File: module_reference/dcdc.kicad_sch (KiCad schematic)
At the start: 59 parts, among them J301 Conn_01x01, J302 Conn_01x01, J303 Conn_01x01, J304 Conn_01x01, J305 Conn_01x01, Q301 MMBT3904, T301 Feryster RTN-40x25x15(M-083), U301 L78L33_SOT89, U302 LT3439, U303 24AA02-OT, U304 TMP117, U305 LT3045xMSE

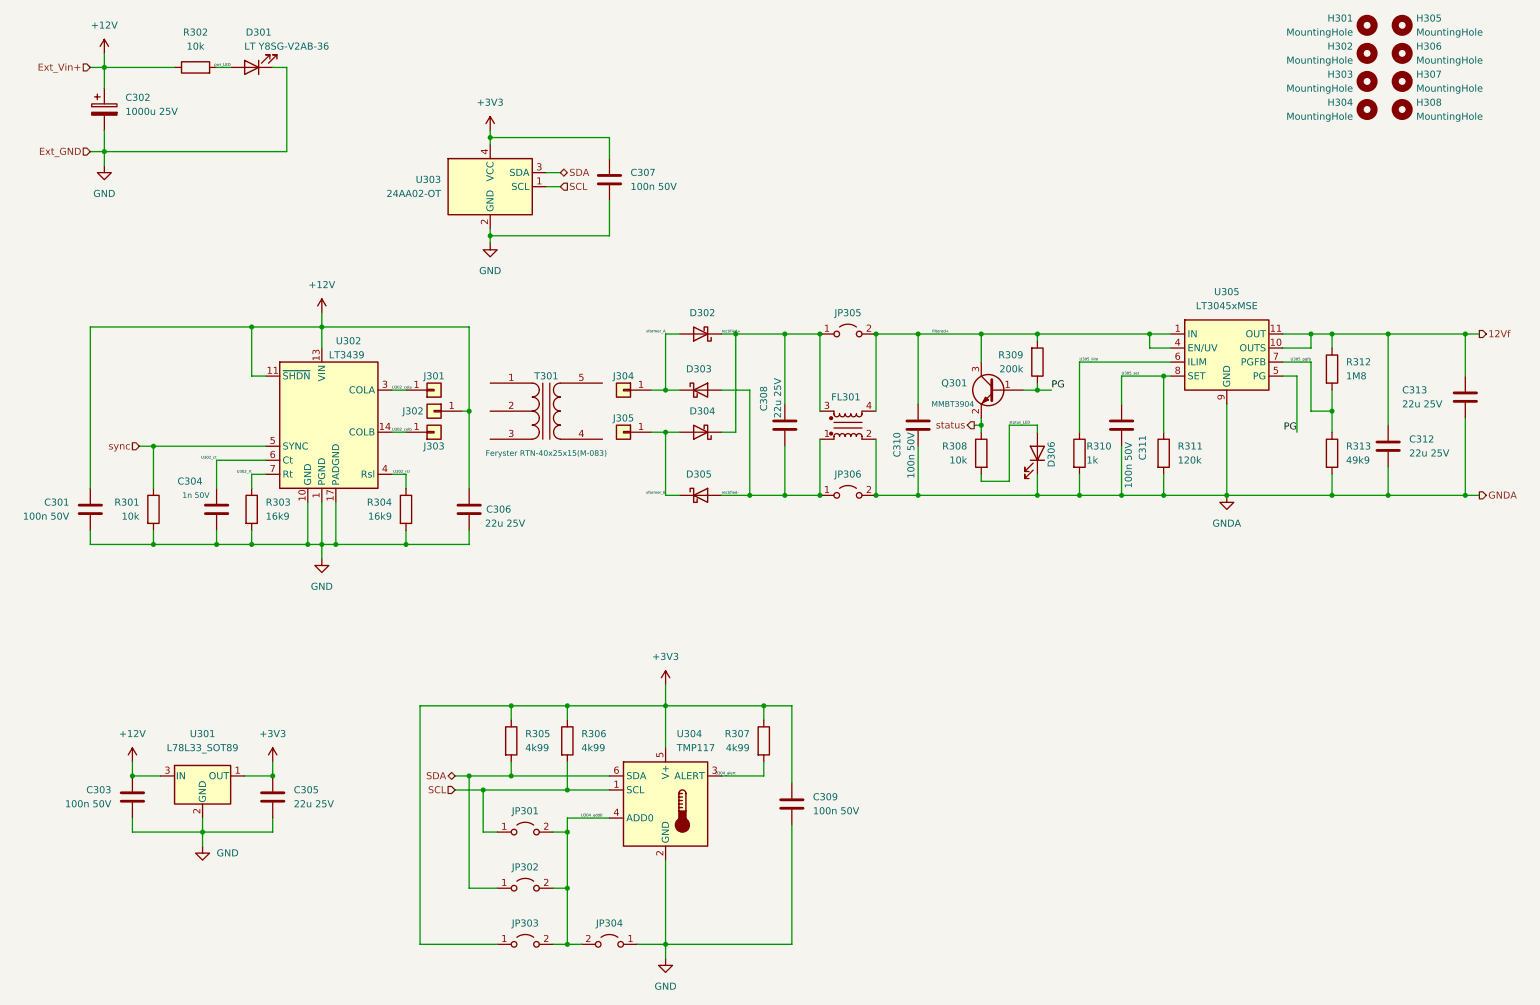
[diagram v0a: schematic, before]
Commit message: switched to addressable eeprom
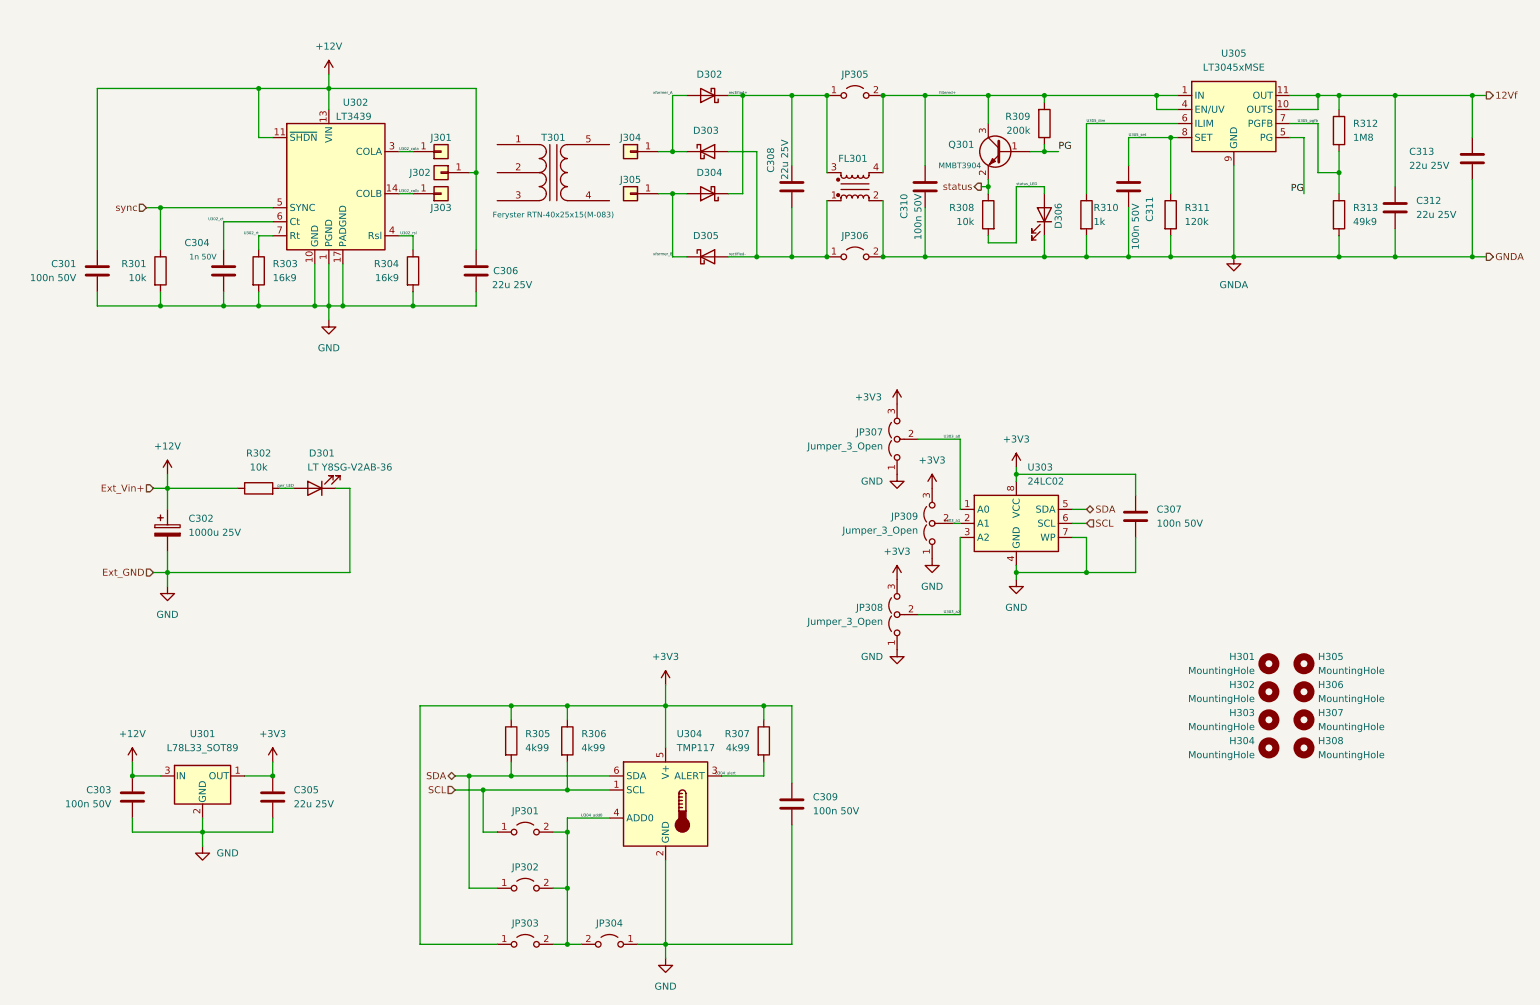
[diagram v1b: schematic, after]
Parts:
- removed U303: 24AA02-OT, Package_TO_SOT_SMD:SOT-23-5, symbol Memory_EEPROM:24AA02-OT
- added JP307, JP308, JP309: Jumper_3_Open, Jumper:SolderJumper-3_P1.3mm_Open_RoundedPad1.0x1.5mm_NumberLabels, symbol Jumper:Jumper_3_Open
- added U303: 24LC02, Package_SO:MSOP-8_3x3mm_P0.65mm, symbol Memory_EEPROM:24LC02
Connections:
- net +3V3: now also JP307.3 (B), JP308.3 (B), JP309.3 (B), U303.8 (VCC)
- net GND: now also JP307.1 (A), JP308.1 (A), JP309.1 (A), U303.4 (GND), U303.7 (WP)
- net SCL: now also U303.6 (SCL)
- net SDA: now also U303.5 (SDA)
- new net U303_a0: JP307.2 (C), U303.1 (A0)
- new net U303_a1: JP309.2 (C), U303.2 (A1)
- new net U303_a2: JP308.2 (C), U303.3 (A2)
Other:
- moved on the sheet: C301, C302, C304, C306, C307, C308, C310, C311, C312, C313, D301, D302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

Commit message: rev 0.4 layout step
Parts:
- removed FL301: B82793C0206N265, ADRmu_Library:Filter_EPCOS_B82793C0, symbol Device:Filter_EMI_CommonMode
- removed JP305, JP306: Jumper_2_Open, Jumper:SolderJumper-2_P1.3mm_Open_RoundedPad1.0x1.5mm, symbol Jumper:Jumper_2_Open
- renumbered C303 to C302, C302 to C303, C308 to C307, C309 to C308, C310 to C309, C311 to C310, C307 to C311, R303 to R302, R302 to R303, U304 to U303, U303 to U304
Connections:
- net rectified+ is gone; now on net filtered+: C307.1, D302.1 (K), D304.1 (K)
- net rectified- is gone; now on net GNDA: C307.2, D303.2 (A), D305.2 (A)
- no-connect marks 0 -> 5
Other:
- moved on the sheet: C309, C310, C312, C313, D306, Q301, R308, R309, R310, R311, R312, R313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

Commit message: asdf
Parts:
- JP307, JP308, JP309: now left out of the parts list
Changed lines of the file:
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@@
   (title_block
     (title "DC-DC converter & misc")
-    (date "2022-03-02")
+    (date "2022-03-04")
     (rev "0.4")
     (company "RPG")
@@
   )
   (symbol (lib_id "Jumper:Jumper_3_Open") (at 171.45 92.71 90) (unit 1)
-    (in_bom yes) (on_board yes) (fields_autoplaced)
+    (in_bom no) (on_board yes) (fields_autoplaced)
     (property "Reference" "JP307" (id 0) (at 168.91 91.4399 90)
       (effects (font (size 1.27 1.27)) (justify left))
@@
   )
   (symbol (lib_id "Jumper:Jumper_3_Open") (at 177.8 107.95 90) (unit 1)
-    (in_bom yes) (on_board yes) (fields_autoplaced)
+    (in_bom no) (on_board yes) (fields_autoplaced)
     (property "Reference" "JP309" (id 0) (at 175.26 106.6799 90)
       (effects (font (size 1.27 1.27)) (justify left))
@@
   )
   (symbol (lib_id "Jumper:Jumper_3_Open") (at 171.45 124.46 90) (unit 1)
-    (in_bom yes) (on_board yes) (fields_autoplaced)
+    (in_bom no) (on_board yes) (fields_autoplaced)
     (property "Reference" "JP308" (id 0) (at 168.91 123.1899 90)
       (effects (font (size 1.27 1.27)) (justify left))

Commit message: dimmed LED brightness and started to fix a few first generation battery bug fixes
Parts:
- R303, R308: value 10k -> 16k9
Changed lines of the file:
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@@
     (in_bom yes) (on_board yes) (fields_autoplaced)
     (property "Reference" "R303" (id 0) (at 55.88 95.25 90))
-    (property "Value" "10k" (id 1) (at 55.88 97.79 90))
+    (property "Value" "16k9" (id 1) (at 55.88 97.79 90))
     (property "Footprint" "Resistor_SMD:R_0805_2012Metric" (id 2) (at 55.88 103.378 90)
       (effects (font (size 1.27 1.27)) hide)
@@
       (effects (font (size 1.27 1.27)) (justify left))
     )
-    (property "Value" "10k" (id 1) (at 168.91 53.3399 0)
-      (effects (font (size 1.27 1.27)) (justify left))
-    )
+    (property "Value" "16k9" (id 1) (at 168.91 53.3399 0)
+      (effects (font (size 1.27 1.27)) (justify left))
+    )

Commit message: Battery module Rev 0.2
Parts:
- C303: value 1000u 25V -> 470u 25V
- R303, R308: value 16k9 -> 49k9
- U304: value 24LC02 -> BR24H64FVM
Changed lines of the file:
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@@
       (effects (font (size 1.27 1.27)) (justify left))
     )
-    (property "Value" "24LC02" (id 1) (at 195.0594 100.33 0)
+    (property "Value" "BR24H64FVM" (id 1) (at 195.0594 100.33 0)
       (effects (font (size 1.27 1.27)) (justify left))
     )
@@
       (effects (font (size 1.27 1.27)) hide)
     )
-    (property "Datasheet" "http://ww1.microchip.com/downloads/en/DeviceDoc/21709c.pdf" (id 3) (at 193.04 107.95 0)
+    (property "Datasheet" "https://fscdn.rohm.com/en/products/databook/datasheet/ic/memory/eeprom/br24h64xxx-5ac-e.pdf" (id 3) (at 193.04 107.95 0)
       (effects (font (size 1.27 1.27)) hide)
     )
@@
       (effects (font (size 1.27 1.27)) (justify left))
     )
-    (property "Value" "1000u 25V" (id 1) (at 43.18 109.6009 0)
+    (property "Value" "470u 25V" (id 1) (at 43.18 109.6009 0)
       (effects (font (size 1.27 1.27)) (justify left))
     )
@@
     (in_bom yes) (on_board yes) (fields_autoplaced)
     (property "Reference" "R303" (id 0) (at 55.88 95.25 90))
-    (property "Value" "16k9" (id 1) (at 55.88 97.79 90))
+    (property "Value" "49k9" (id 1) (at 55.88 97.79 90))
     (property "Footprint" "Resistor_SMD:R_0805_2012Metric" (id 2) (at 55.88 103.378 90)
       (effects (font (size 1.27 1.27)) hide)
@@
       (effects (font (size 1.27 1.27)) (justify left))
     )
-    (property "Value" "16k9" (id 1) (at 168.91 53.3399 0)
-      (effects (font (size 1.27 1.27)) (justify left))
-    )
+    (property "Value" "49k9" (id 1) (at 168.91 53.3399 0)
+      (effects (font (size 1.27 1.27)) (justify left))
+    )

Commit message: asdf
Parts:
- renumbered JP307 to JP305, JP308 to JP306, JP309 to JP307
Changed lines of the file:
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@@
   (symbol (lib_id "Jumper:Jumper_3_Open") (at 171.45 92.71 90) (unit 1)
     (in_bom no) (on_board yes) (fields_autoplaced)
-    (property "Reference" "JP307" (id 0) (at 168.91 91.4399 90)
+    (property "Reference" "JP305" (id 0) (at 168.91 91.4399 90)
       (effects (font (size 1.27 1.27)) (justify left))
     )
@@
   (symbol (lib_id "Jumper:Jumper_3_Open") (at 177.8 107.95 90) (unit 1)
     (in_bom no) (on_board yes) (fields_autoplaced)
-    (property "Reference" "JP309" (id 0) (at 175.26 106.6799 90)
+    (property "Reference" "JP307" (id 0) (at 175.26 106.6799 90)
       (effects (font (size 1.27 1.27)) (justify left))
     )
@@
   (symbol (lib_id "Jumper:Jumper_3_Open") (at 171.45 124.46 90) (unit 1)
     (in_bom no) (on_board yes) (fields_autoplaced)
-    (property "Reference" "JP308" (id 0) (at 168.91 123.1899 90)
-      (effects (font (size 1.27 1.27)) (justify left))
-    )
+    (property "Reference" "JP306" (id 0) (at 168.91 123.1899 90)
+      (effects (font (size 1.27 1.27)) (justify left))
+    )

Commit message: asdf
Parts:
- R311: value 120k -> 110k
- R312: value 1M8 -> 1M
- R313: value 49k9 -> 30k
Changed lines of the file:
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@@
       (effects (font (size 1.27 1.27)) (justify left))
     )
-    (property "Value" "120k" (id 1) (at 207.01 53.3399 0)
+    (property "Value" "110k" (id 1) (at 207.01 53.3399 0)
       (effects (font (size 1.27 1.27)) (justify left))
     )
@@
       (effects (font (size 1.27 1.27)) (justify left))
     )
-    (property "Value" "49k9" (id 1) (at 237.49 53.3399 0)
+    (property "Value" "30k" (id 1) (at 237.49 53.3399 0)
       (effects (font (size 1.27 1.27)) (justify left))
     )
@@
       (effects (font (size 1.27 1.27)) (justify left))
     )
-    (property "Value" "1M8" (id 1) (at 237.49 38.0999 0)
-      (effects (font (size 1.27 1.27)) (justify left))
-    )
+    (property "Value" "1M" (id 1) (at 237.49 38.0999 0)
+      (effects (font (size 1.27 1.27)) (justify left))
+    )

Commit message: Reference board Rev 0.5 schematic
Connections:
- net U303_a0 renamed U304_a0
- net U303_a1 renamed U304_a1
- net U303_a2 renamed U304_a2
- net U304_add0 renamed U303_add0
- net U304_alert renamed U303_alert
- net filtered+ renamed rectified+
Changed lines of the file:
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@@
   (title_block
     (title "DC-DC converter & misc")
-    (date "2022-03-04")
-    (rev "0.4")
+    (date "2022-05-22")
+    (rev "0.5")
     (company "RPG")
     (comment 1 "All resistors 0.1% MF unless otherwise noted")
@@
   )
   (junction (at 58.42 153.67) (diameter 0) (color 0 0 0 0)
-  )
-  (junction (at 171.45 46.99) (diameter 0) (color 0 0 0 0)
   )
   (junction (at 39.37 116.84) (diameter 0) (color 0 0 0 0)
@@
     (stroke (width 0) (type default) (color 0 0 0 0))
   )
-  (wire (pts (xy 170.18 46.99) (xy 171.45 46.99))
-    (stroke (width 0) (type default) (color 0 0 0 0))
-  )
   (wire (pts (xy 38.1 68.58) (xy 49.53 68.58))
     (stroke (width 0) (type default) (color 0 0 0 0))
@@
     (stroke (width 0) (type default) (color 0 0 0 0))
   )
-  (wire (pts (xy 171.45 46.99) (xy 171.45 45.72))
+  (wire (pts (xy 171.45 45.72) (xy 171.45 48.26))
     (stroke (width 0) (type default) (color 0 0 0 0))
   )
@@
   )
   (wire (pts (xy 171.45 30.48) (xy 181.61 30.48))
-    (stroke (width 0) (type default) (color 0 0 0 0))
-  )
-  (wire (pts (xy 171.45 48.26) (xy 171.45 46.99))
     (stroke (width 0) (type default) (color 0 0 0 0))
   )
@@
     (effects (font (size 0.5 0.5)) (justify right bottom))
   )
-  (label "U303_a0" (at 182.88 92.71 180)
+  (label "U304_a0" (at 182.88 92.71 180)
     (effects (font (size 0.5 0.5)) (justify right bottom))
   )
@@
     (effects (font (size 0.5 0.5)) (justify right bottom))
   )
-  (label "rectified-" (at 140.97 59.69 0)
-    (effects (font (size 0.5 0.5)) (justify left bottom))
-  )
-  (label "U304_alert" (at 142.24 153.67 180)
+  (label "U303_alert" (at 142.24 153.67 180)
     (effects (font (size 0.5 0.5)) (justify right bottom))
   )
@@
     (effects (font (size 0.5 0.5)) (justify left bottom))
   )
-  (label "U303_a1" (at 182.88 107.95 180)
+  (label "U304_a1" (at 182.88 107.95 180)
     (effects (font (size 0.5 0.5)) (justify right bottom))
-  )
-  (label "filtered+" (at 162.56 30.48 0)
-    (effects (font (size 0.5 0.5)) (justify left bottom))
   )
   (label "U305_set" (at 196.85 38.1 0)
     (effects (font (size 0.5 0.5)) (justify left bottom))
   )
+  (label "status" (at 171.45 46.99 180)
+    (effects (font (size 0.5 0.5)) (justify right bottom))
+  )
   (label "U302_cola" (at 81.28 40.64 0)
     (effects (font (size 0.5 0.5)) (justify left bottom))
@@
     (effects (font (size 0.5 0.5)) (justify left bottom))
   )
-  (label "U303_a2" (at 182.88 124.46 180)
+  (label "U304_a2" (at 182.88 124.46 180)
     (effects (font (size 0.5 0.5)) (justify right bottom))
   )
@@
     (effects (font (size 0.5 0.5)) (justify right bottom))
   )
-  (label "U304_add0" (at 118.11 161.29 180)
+  (label "U303_add0" (at 118.11 161.29 180)
     (effects (font (size 0.5 0.5)) (justify right bottom))
   )
@@
     (effects (font (size 1.27 1.27)) (justify left))
   )
-  (hierarchical_label "status" (shape output) (at 170.18 46.99 180)
-    (effects (font (size 1.27 1.27)) (justify right))
-  )
   (hierarchical_label "SCL" (shape input) (at 91.44 156.21 180)
     (effects (font (size 1.27 1.27)) (justify right))
@@
     (effects (font (size 1.27 1.27)) (justify right))
   )
-  (hierarchical_label "Ext_GND" (shape input) (at 36.83 116.84 180)
+  (hierarchical_label "GND" (shape input) (at 36.83 116.84 180)
     (effects (font (size 1.27 1.27)) (justify right))
   )
@@
     (effects (font (size 1.27 1.27)) (justify right))
   )
-  (hierarchical_label "Ext_Vin+" (shape input) (at 36.83 101.6 180)
+  (hierarchical_label "+12V" (shape input) (at 36.83 101.6 180)
     (effects (font (size 1.27 1.27)) (justify right))
   )
@@
       (effects (font (size 1.27 1.27)) hide)
     )
-    (property "Datasheet" "https://fscdn.rohm.com/en/products/databook/datasheet/ic/memory/eeprom/br24h64xxx-5ac-e.pdf" (id 3) (at 193.04 107.95 0)
+    (property "Datasheet" "http://ww1.microchip.com/downloads/en/DeviceDoc/21709c.pdf" (id 3) (at 193.04 107.95 0)
       (effects (font (size 1.27 1.27)) hide)
     )
@@
     (pin "2")
   )
+  (symbol (lib_id "power:PWR_FLAG") (at 146.05 59.69 180) (unit 1)
+    (in_bom yes) (on_board yes) (fields_autoplaced)
+    (property "Reference" "#FLG0103" (id 0) (at 146.05 61.595 0)
+      (effects (font (size 1.27 1.27)) hide)
+    )
+    (property "Value" "PWR_FLAG" (id 1) (at 146.05 64.77 0))
+    (property "Footprint" "" (id 2) (at 146.05 59.69 0)
+      (effects (font (size 1.27 1.27)) hide)
+    )
+    (property "Datasheet" "~" (id 3) (at 146.05 59.69 0)
+      (effects (font (size 1.27 1.27)) hide)
+    )
+    (pin "1")
+  )
   (symbol (lib_id "Device:C") (at 214.63 106.68 0) (unit 1)
     (in_bom yes) (on_board yes) (fields_autoplaced)
@@
       (effects (font (size 1.27 1.27)) hide)
     )
+    (pin "1")
+  )
+  (symbol (lib_id "power:PWR_FLAG") (at 143.51 30.48 0) (unit 1)
+    (in_bom yes) (on_board yes) (fields_autoplaced)
+    (property "Reference" "#FLG0102" (id 0) (at 143.51 28.575 0)
+      (effects (font (size 1.27 1.27)) hide)
+    )
+    (property "Value" "PWR_FLAG" (id 1) (at 143.51 25.4 0))
+    (property "Footprint" "" (id 2) (at 143.51 30.48 0)
+      (effects (font (size 1.27 1.27)) hide)
+    )
+    (property "Datasheet" "~" (id 3) (at 143.51 30.48 0)
+      (effects (font (size 1.27 1.27)) hide)
+    )
